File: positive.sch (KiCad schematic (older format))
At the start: 33 parts, among them U1 NE555, U2 IXDF604SIA, U3 FOD8316, U6 Transformer_2P_2S

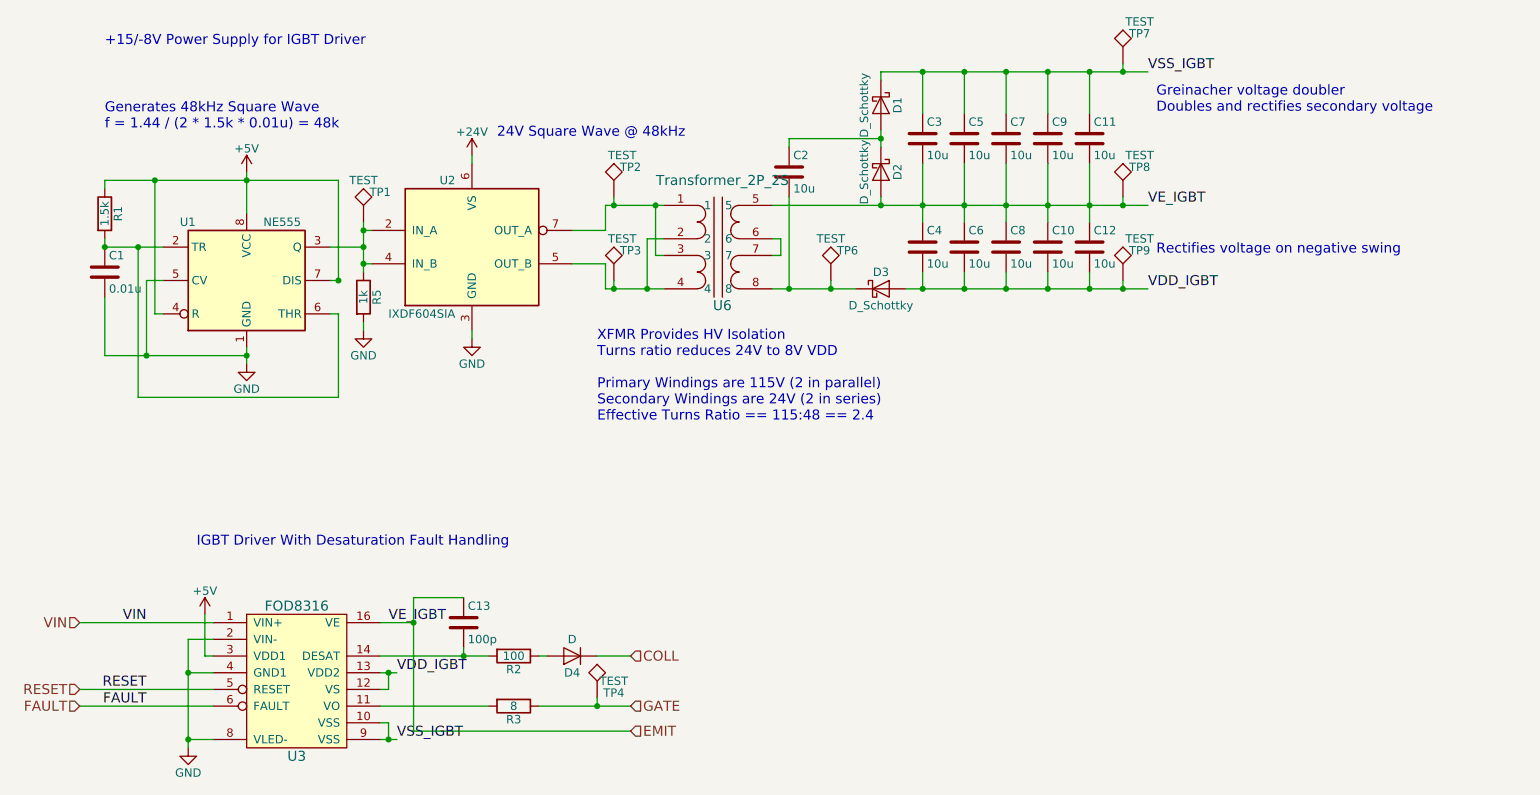
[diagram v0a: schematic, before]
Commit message: Including both igbt drivers on one board.
WIP
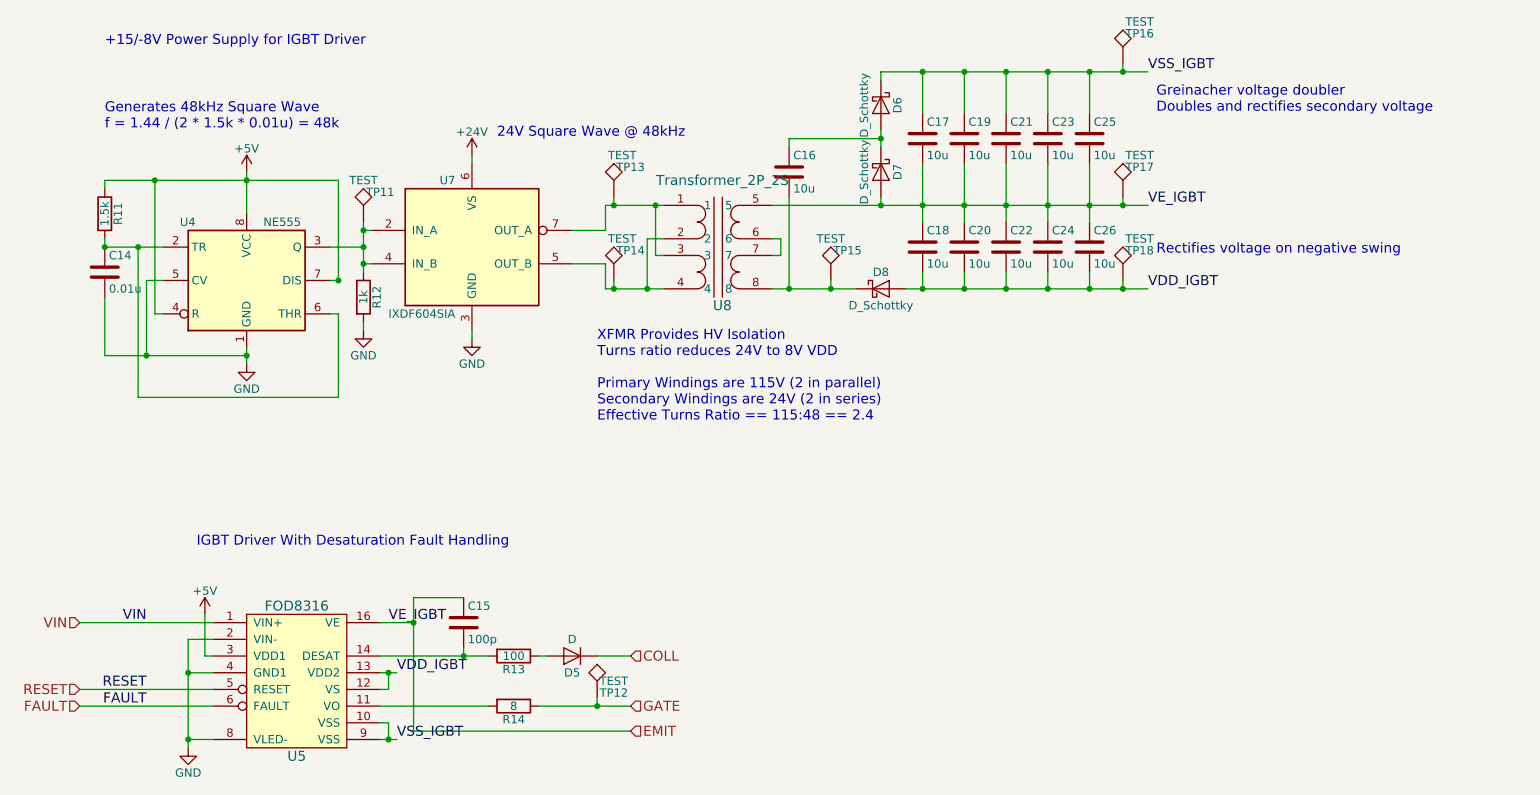
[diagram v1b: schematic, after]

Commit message: Move square wave generator to single module.
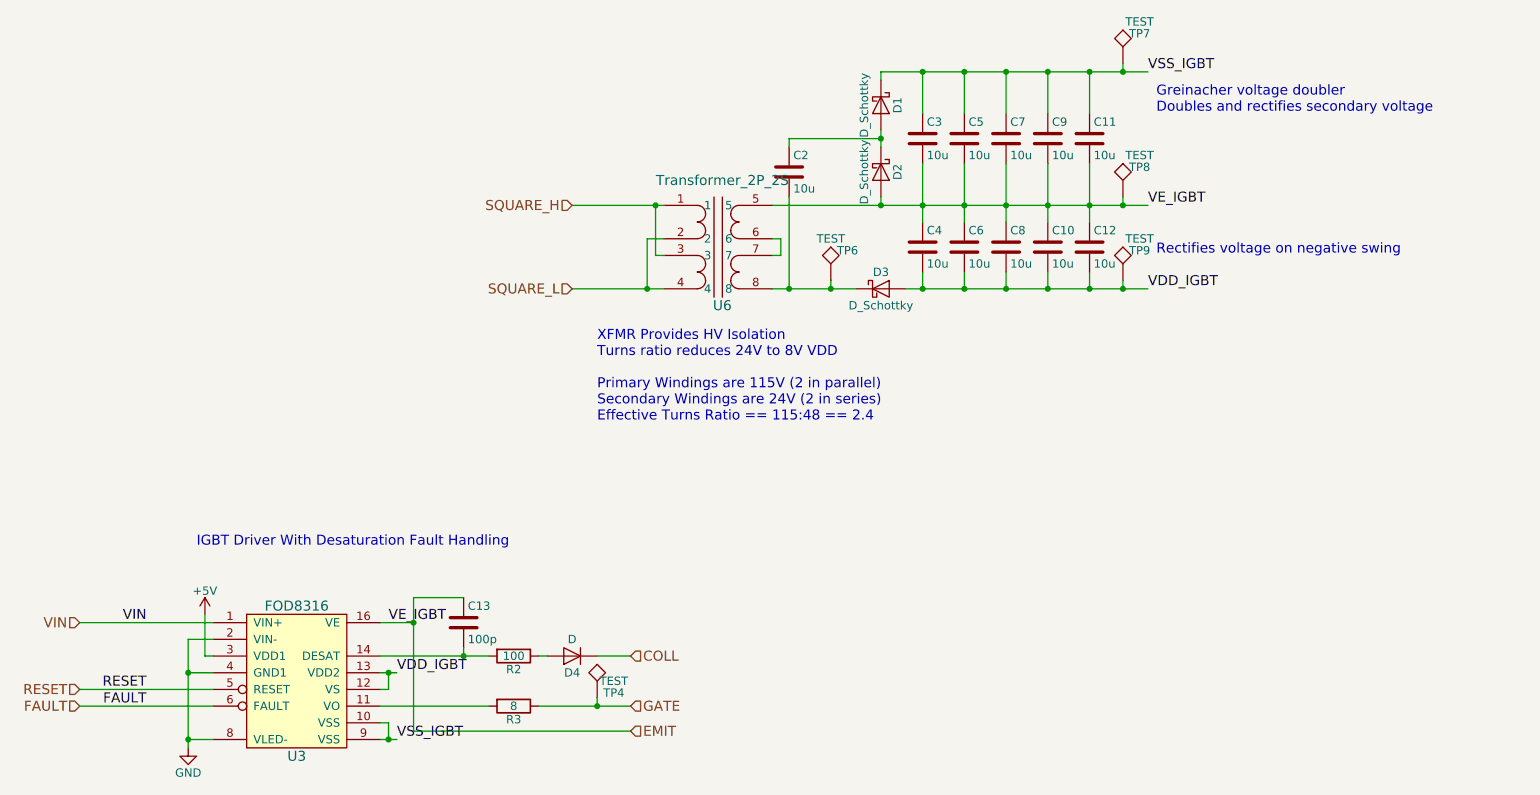
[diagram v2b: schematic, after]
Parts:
- removed C1: 0.01u, Capacitors_SMD:C_0603_HandSoldering, symbol C
- removed R1: 1.5k, Resistors_SMD:R_0603_HandSoldering, symbol R
- removed R5: 1k, Resistors_SMD:R_0402, symbol R
- removed TP1, TP2, TP3: TEST, inverter-igbt-driver:TP RCT (0805), symbol TEST
- removed U1: NE555, Housings_SOIC:SOIC-8_3.9x4.9mm_Pitch1.27mm, symbol NE555
- removed U2: IXDF604SIA, Housings_SOIC:SOIC-8_3.9x4.9mm_Pitch1.27mm, symbol IXDF604SIA
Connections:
- net SQUARE_L: now reaches U6.2, U6.4
- net SQUARE_H: now reaches U6.1, U6.3
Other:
- note removed: "+15/-8V Power Supply for IGBT Driver\n"
- note removed: "24V Square Wave @ 48kHz"
- note removed: "Generates 48kHz Square Wave\nf = 1.44 / (2 * 1.5k * 0.01u) = 48k"

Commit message: Completed layout with one connector.
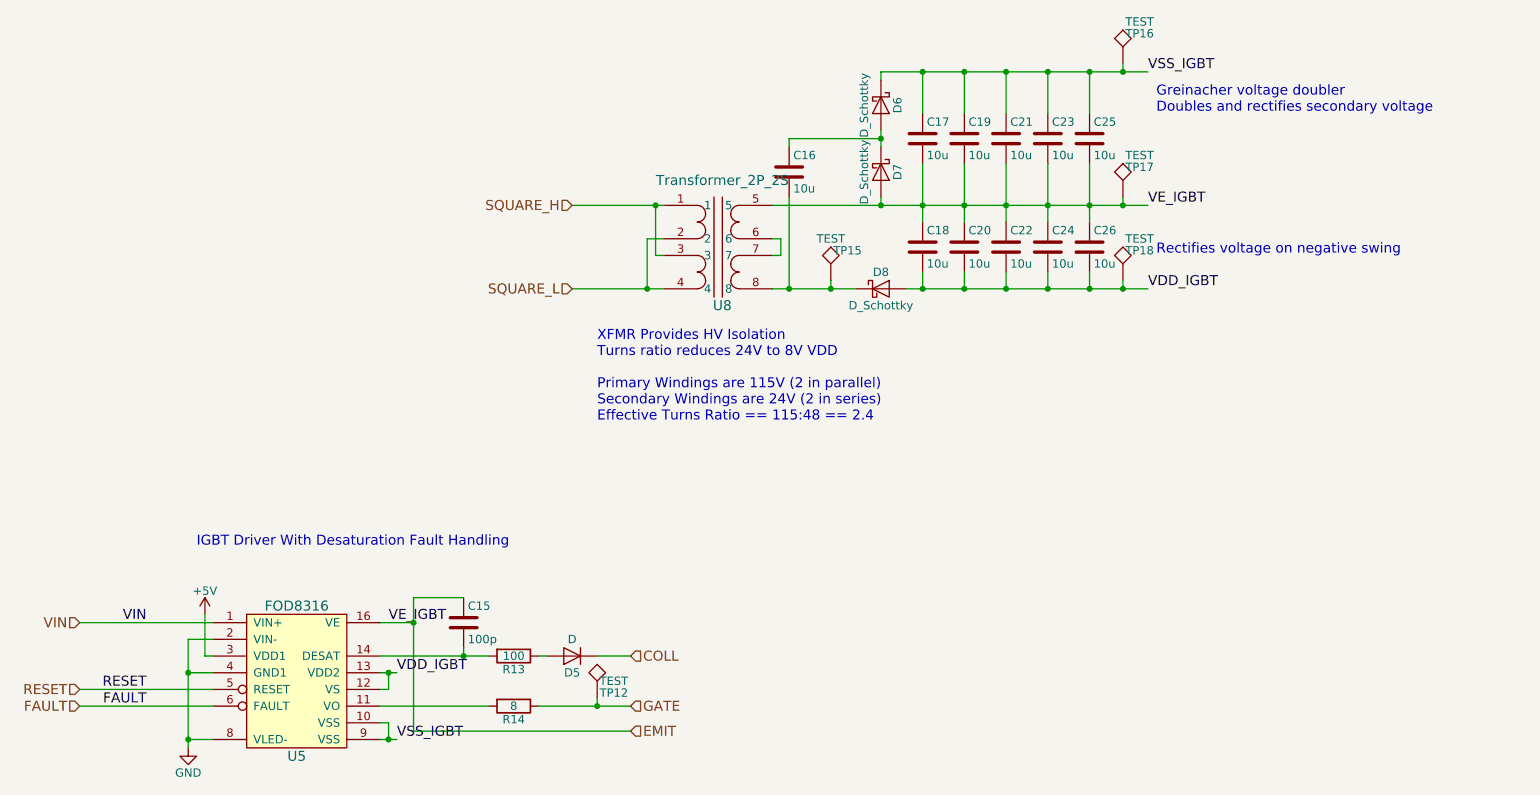
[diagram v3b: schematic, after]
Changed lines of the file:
@@
 AR Path="/5AD96A61/5AD97D83" Ref="C4"  Part="1"
 AR Path="/5ADA6656/5AD97D83" Ref="C18"  Part="1"
-F 0 "C4" H 6325 2400 50  0000 L CNN
+F 0 "C18" H 6325 2400 50  0000 L CNN
 F 1 "10u" H 6325 2200 50  0000 L CNN
 F 2 "Capacitors_SMD:C_1206_HandSoldering" H 6338 2150 50  0001 C CNN
@@
 AR Path="/5AD96A61/5AD97D8A" Ref="C3"  Part="1"
 AR Path="/5ADA6656/5AD97D8A" Ref="C17"  Part="1"
-F 0 "C3" H 6325 1750 50  0000 L CNN
+F 0 "C17" H 6325 1750 50  0000 L CNN
 F 1 "10u" H 6325 1550 50  0000 L CNN
 F 2 "Capacitors_SMD:C_1206_HandSoldering" H 6338 1500 50  0001 C CNN
@@
 AR Path="/5AD96A61/5AD97D91" Ref="C2"  Part="1"
 AR Path="/5ADA6656/5AD97D91" Ref="C16"  Part="1"
-F 0 "C2" H 5525 1950 50  0000 L CNN
+F 0 "C16" H 5525 1950 50  0000 L CNN
 F 1 "10u" H 5525 1750 50  0000 L CNN
 F 2 "Capacitors_SMD:C_1206_HandSoldering" H 5538 1700 50  0001 C CNN
@@
 AR Path="/5AD96A61/5AD97D98" Ref="D2"  Part="1"
 AR Path="/5ADA6656/5AD97D98" Ref="D7"  Part="1"
-F 0 "D2" H 6050 1950 50  0000 C CNN
+F 0 "D7" H 6050 1950 50  0000 C CNN
 F 1 "D_Schottky" H 6050 1750 50  0000 C CNN
 F 2 "Diodes_SMD:D_SOD-123F" H 6050 1850 50  0001 C CNN
@@
 AR Path="/5AD96A61/5AD97D9F" Ref="D1"  Part="1"
 AR Path="/5ADA6656/5AD97D9F" Ref="D6"  Part="1"
-F 0 "D1" H 6050 1550 50  0000 C CNN
+F 0 "D6" H 6050 1550 50  0000 C CNN
 F 1 "D_Schottky" H 6050 1350 50  0000 C CNN
 F 2 "Diodes_SMD:D_SOD-123F" H 6050 1450 50  0001 C CNN
@@
 AR Path="/5AD96A61/5AD97DA6" Ref="D3"  Part="1"
 AR Path="/5ADA6656/5AD97DA6" Ref="D8"  Part="1"
-F 0 "D3" H 6050 2650 50  0000 C CNN
+F 0 "D8" H 6050 2650 50  0000 C CNN
 F 1 "D_Schottky" H 6050 2450 50  0000 C CNN
 F 2 "Diodes_SMD:D_SOD-123F" H 6050 2550 50  0001 C CNN
@@
 AR Path="/5AD96A61/5AD97DE9" Ref="C5"  Part="1"
 AR Path="/5ADA6656/5AD97DE9" Ref="C19"  Part="1"
-F 0 "C5" H 6575 1750 50  0000 L CNN
+F 0 "C19" H 6575 1750 50  0000 L CNN
 F 1 "10u" H 6575 1550 50  0000 L CNN
 F 2 "Capacitors_SMD:C_1206_HandSoldering" H 6588 1500 50  0001 C CNN
@@
 AR Path="/5AD96A61/5AD97DF0" Ref="C7"  Part="1"
 AR Path="/5ADA6656/5AD97DF0" Ref="C21"  Part="1"
-F 0 "C7" H 6825 1750 50  0000 L CNN
+F 0 "C21" H 6825 1750 50  0000 L CNN
 F 1 "10u" H 6825 1550 50  0000 L CNN
 F 2 "Capacitors_SMD:C_1206_HandSoldering" H 6838 1500 50  0001 C CNN
@@
 AR Path="/5AD96A61/5AD97DF7" Ref="C9"  Part="1"
 AR Path="/5ADA6656/5AD97DF7" Ref="C23"  Part="1"
-F 0 "C9" H 7075 1750 50  0000 L CNN
+F 0 "C23" H 7075 1750 50  0000 L CNN
 F 1 "10u" H 7075 1550 50  0000 L CNN
 F 2 "Capacitors_SMD:C_1206_HandSoldering" H 7088 1500 50  0001 C CNN
@@
 AR Path="/5AD96A61/5AD97DFE" Ref="C11"  Part="1"
 AR Path="/5ADA6656/5AD97DFE" Ref="C25"  Part="1"
-F 0 "C11" H 7325 1750 50  0000 L CNN
+F 0 "C25" H 7325 1750 50  0000 L CNN
 F 1 "10u" H 7325 1550 50  0000 L CNN
 F 2 "Capacitors_SMD:C_1206_HandSoldering" H 7338 1500 50  0001 C CNN
@@
 AR Path="/5AD96A61/5AD97E05" Ref="C6"  Part="1"
 AR Path="/5ADA6656/5AD97E05" Ref="C20"  Part="1"
-F 0 "C6" H 6575 2400 50  0000 L CNN
+F 0 "C20" H 6575 2400 50  0000 L CNN
 F 1 "10u" H 6575 2200 50  0000 L CNN
 F 2 "Capacitors_SMD:C_1206_HandSoldering" H 6588 2150 50  0001 C CNN
@@
 AR Path="/5AD96A61/5AD97E0C" Ref="C8"  Part="1"
 AR Path="/5ADA6656/5AD97E0C" Ref="C22"  Part="1"
-F 0 "C8" H 6825 2400 50  0000 L CNN
+F 0 "C22" H 6825 2400 50  0000 L CNN
 F 1 "10u" H 6825 2200 50  0000 L CNN
 F 2 "Capacitors_SMD:C_1206_HandSoldering" H 6838 2150 50  0001 C CNN
@@
 AR Path="/5AD96A61/5AD97E13" Ref="C10"  Part="1"
 AR Path="/5ADA6656/5AD97E13" Ref="C24"  Part="1"
-F 0 "C10" H 7075 2400 50  0000 L CNN
+F 0 "C24" H 7075 2400 50  0000 L CNN
 F 1 "10u" H 7075 2200 50  0000 L CNN
 F 2 "Capacitors_SMD:C_1206_HandSoldering" H 7088 2150 50  0001 C CNN
@@
 AR Path="/5AD96A61/5AD97E1A" Ref="C12"  Part="1"
 AR Path="/5ADA6656/5AD97E1A" Ref="C26"  Part="1"
-F 0 "C12" H 7325 2400 50  0000 L CNN
+F 0 "C26" H 7325 2400 50  0000 L CNN
 F 1 "10u" H 7325 2200 50  0000 L CNN
 F 2 "Capacitors_SMD:C_1206_HandSoldering" H 7338 2150 50  0001 C CNN
@@
 AR Path="/5AD96A61/5AD97E37" Ref="TP6"  Part="1"
 AR Path="/5ADA6656/5AD97E37" Ref="TP15"  Part="1"
-F 0 "TP6" H 5850 2650 50  0000 C BNN
+F 0 "TP15" H 5850 2650 50  0000 C BNN
 F 1 "TEST" H 5750 2750 50  0000 C CNN
 F 2 "inverter-igbt-driver:TP RCT (0805)" H 5750 2500 50  0001 C CNN
@@
 AR Path="/5AD96A61/5AD97E3E" Ref="TP7"  Part="1"
 AR Path="/5ADA6656/5AD97E3E" Ref="TP16"  Part="1"
-F 0 "TP7" H 7600 1350 50  0000 C BNN
+F 0 "TP16" H 7600 1350 50  0000 C BNN
 F 1 "TEST" H 7600 1450 50  0000 C CNN
 F 2 "inverter-igbt-driver:TP RCT (0805)" H 7500 1200 50  0001 C CNN
@@
 AR Path="/5AD96A61/5AD97E45" Ref="TP8"  Part="1"
 AR Path="/5ADA6656/5AD97E45" Ref="TP17"  Part="1"
-F 0 "TP8" H 7600 2150 50  0000 C BNN
+F 0 "TP17" H 7600 2150 50  0000 C BNN
 F 1 "TEST" H 7600 2250 50  0000 C CNN
 F 2 "inverter-igbt-driver:TP RCT (0805)" H 7500 2000 50  0001 C CNN
@@
 AR Path="/5AD96A61/5AD97E4C" Ref="TP9"  Part="1"
 AR Path="/5ADA6656/5AD97E4C" Ref="TP18"  Part="1"
-F 0 "TP9" H 7600 2650 50  0000 C BNN
+F 0 "TP18" H 7600 2650 50  0000 C BNN
 F 1 "TEST" H 7600 2750 50  0000 C CNN
 F 2 "inverter-igbt-driver:TP RCT (0805)" H 7500 2500 50  0001 C CNN
@@
 AR Path="/5AD96A61/5AD97E53" Ref="U6"  Part="1"
 AR Path="/5ADA6656/5AD97E53" Ref="U8"  Part="1"
-F 0 "U6" H 5100 1650 60  0000 C CNN
+F 0 "U8" H 5100 1650 60  0000 C CNN
 F 1 "Transformer_2P_2S" H 5100 2400 60  0000 C CNN
 F 2 "inverter-igbt-driver:FS48-050-C2" H 5100 2150 60  0001 C CNN
@@
 AR Path="/5AD96A61/5AD9846B" Ref="U3"  Part="1"
 AR Path="/5ADA6656/5AD9846B" Ref="U5"  Part="1"
-F 0 "U3" H 2550 4450 60  0000 C CNN
+F 0 "U5" H 2550 4450 60  0000 C CNN
 F 1 "FOD8316" H 2550 5350 60  0000 C CNN
 F 2 "Housings_SOIC:SOIC-16W_7.5x10.3mm_Pitch1.27mm" H 2450 4950 60  0001 C CNN
@@
 $EndComp
 $Comp
-L +5V #PWR05
+L +5V #PWR03
 U 1 1 5AD98472
 P 2000 4500
-AR Path="/5AD96A61/5AD98472" Ref="#PWR05"  Part="1"
-AR Path="/5ADA6656/5AD98472" Ref="#PWR07"  Part="1"
+AR Path="/5AD96A61/5AD98472" Ref="#PWR03"  Part="1"
+AR Path="/5ADA6656/5AD98472" Ref="#PWR05"  Part="1"
 F 0 "#PWR05" H 2000 4350 50  0001 C CNN
 F 1 "+5V" H 2000 4640 50  0000 C CNN
@@
 $EndComp
 $Comp
-L GND #PWR06
+L GND #PWR04
 U 1 1 5AD98478
 P 1900 5300
-AR Path="/5AD96A61/5AD98478" Ref="#PWR06"  Part="1"
-AR Path="/5ADA6656/5AD98478" Ref="#PWR08"  Part="1"
+AR Path="/5AD96A61/5AD98478" Ref="#PWR04"  Part="1"
+AR Path="/5ADA6656/5AD98478" Ref="#PWR06"  Part="1"
 F 0 "#PWR06" H 1900 5050 50  0001 C CNN
 F 1 "GND" H 1900 5150 50  0000 C CNN
@@
 AR Path="/5AD96A61/5AD98484" Ref="R3"  Part="1"
 AR Path="/5ADA6656/5AD98484" Ref="R14"  Part="1"
-F 0 "R3" V 3930 5050 50  0000 C CNN
+F 0 "R14" V 3930 5050 50  0000 C CNN
 F 1 "8" V 3850 5050 50  0000 C CNN
 F 2 "Resistors_THT:R_Axial_DIN0207_L6.3mm_D2.5mm_P7.62mm_Horizontal" V 3780 5050 50  0001 C CNN
@@
 AR Path="/5AD96A61/5AD9848B" Ref="C13"  Part="1"
 AR Path="/5ADA6656/5AD9848B" Ref="C15"  Part="1"
-F 0 "C13" H 3575 4650 50  0000 L CNN
+F 0 "C15" H 3575 4650 50  0000 L CNN
 F 1 "100p" H 3575 4450 50  0000 L CNN
 F 2 "Capacitors_SMD:C_1206_HandSoldering" H 3588 4400 50  0001 C CNN
@@
 AR Path="/5AD96A61/5AD98492" Ref="R2"  Part="1"
 AR Path="/5ADA6656/5AD98492" Ref="R13"  Part="1"
-F 0 "R2" V 3930 4750 50  0000 C CNN
+F 0 "R13" V 3930 4750 50  0000 C CNN
 F 1 "100" V 3850 4750 50  0000 C CNN
 F 2 "Resistors_SMD:R_1206_HandSoldering" V 3780 4750 50  0001 C CNN
@@
 AR Path="/5AD96A61/5AD98499" Ref="D4"  Part="1"
 AR Path="/5ADA6656/5AD98499" Ref="D5"  Part="1"
-F 0 "D4" H 4200 4850 50  0000 C CNN
+F 0 "D5" H 4200 4850 50  0000 C CNN
 F 1 "D" H 4200 4650 50  0000 C CNN
 F 2 "inverter-igbt-driver:DO-214AC" H 4200 4750 50  0001 C CNN
@@
 AR Path="/5AD96A61/5AD984A1" Ref="TP4"  Part="1"
 AR Path="/5ADA6656/5AD984A1" Ref="TP12"  Part="1"
-F 0 "TP4" H 4450 5000 50  0000 C BNN
+F 0 "TP12" H 4450 5000 50  0000 C BNN
 F 1 "TEST" H 4450 5100 50  0000 C CNN
 F 2 "inverter-igbt-driver:TP RCT (0805)" H 4350 5000 50  0001 C CNN
